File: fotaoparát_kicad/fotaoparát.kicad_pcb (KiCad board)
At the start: 4 copper layers, 102 x 52 mm, 109 parts, among them J1 Conn_01x08_Pin, J13 Micro_SD_Card_Det2, J2 Conn_01x12_Pin, J4 BUTTONS, SW1 SW_MEC_5G, SW2 SW_MEC_5G, U1 TLV62569DBV, Y2 Crystal_GND23

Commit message: FInalni doteky. Ted uz jenom opravy {snad}
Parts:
- removed J2: Conn_01x12_Pin, Connector_FFC-FPC:Hirose_FH12-11S-0.5SH_1x11-1MP_P0.50mm_Horizontal
- removed the R8 at (188.2, 113.7)
- added R50: 330R, Resistor_SMD:R_0603_1608Metric, F.Cu at (188.2, 113.5)
- moved C30 1.57 mm to (139.2, 124.6)
- moved C29 1.57 mm to (138.4, 124.6)
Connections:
- ESP32_P4 pad 49: USB_DATA_N -> /USB_DATA_N
- ESP32_P4 pad 50: USB_DATA_P -> /USB_DATA_P
- ESP32_P4 pad 95: unconnected-(ESP32_P4-GPIO52/ADC-Pad95) -> LED_A
- Y2 pad 3: Net-(ESP32_P4-XTAL_N) -> Net-(ESP32_P4-XTAL_P)
- Y2 pad 4: Net-(ESP32_P4-XTAL_P) -> Net-(ESP32_P4-XTAL_N)
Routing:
- net Net-(J2-Pin_6): track 99.8 -> 0.00 mm, vias 2 -> 0
- net LED_A: track 0.00 -> 99.8 mm, vias 0 -> 2
- net I2C_SDA: track 37.9 -> 63.1 mm, vias 2 -> 3
- net I2C_SCL: track 37.6 -> 62.3 mm, vias 2 -> 3
- net GND: track 168.3 -> 174.2 mm, vias 46 -> 45
- net Net-(ESP32_P4-XTAL_N): track 11.0 -> 15.8 mm
- net Net-(J4-Pin_2): track 0.00 -> 3.65 mm, vias 0 -> 1
- net Net-(J2-Pin_1): track 3.65 -> 0.00 mm, vias 1 -> 0
- net unconnected-(C13-Pad2): track 1.31 -> 2.62 mm, vias 1 -> 2
- net Net-(ESP32_P4-XTAL_P): track 11.8 -> 13.0 mm
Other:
- board size 102 x 52 mm -> 102 x 52.8 mm

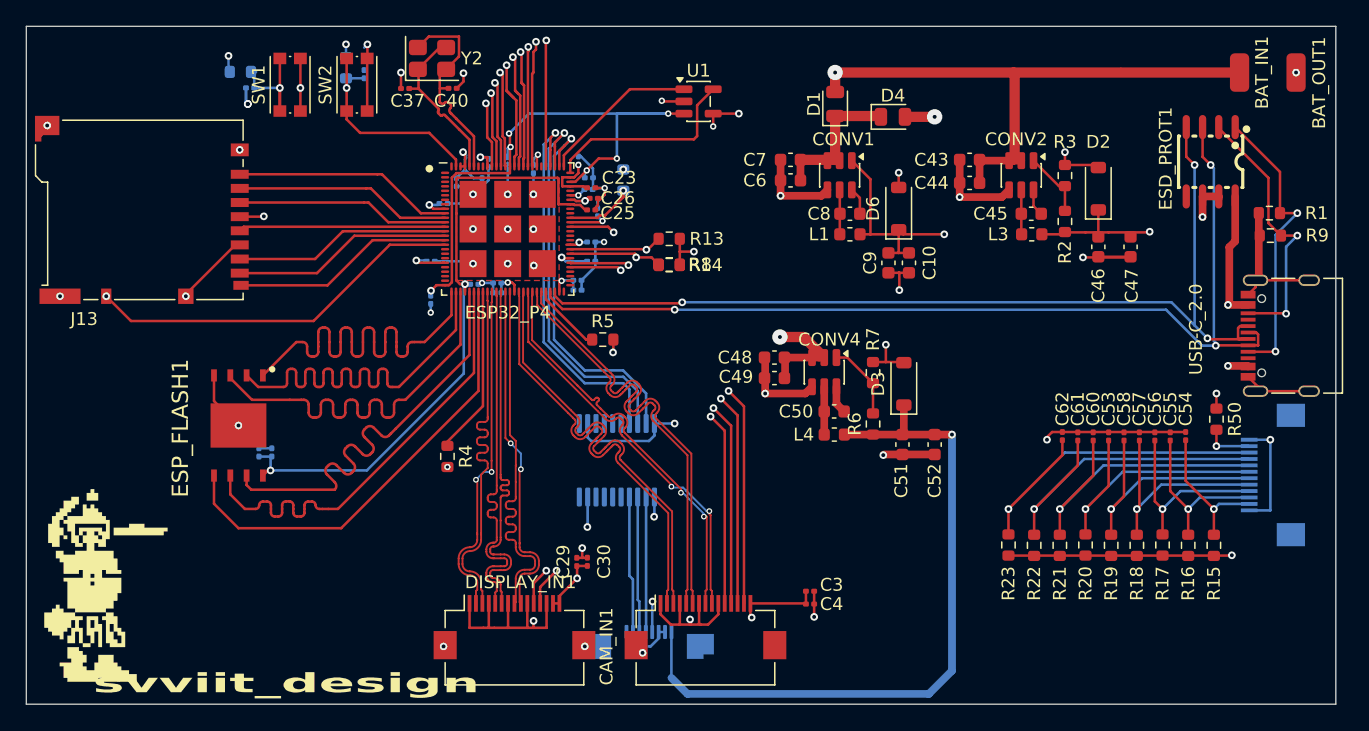
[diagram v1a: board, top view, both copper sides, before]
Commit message: Udelal jsem: -Predelani labelu na global -Pridani vyvodu na desku pro spoust -Pokusil se predelat ten stepdown, Vout by mela byt 1V1, nestihl jsem prepsat vsechny hodnoty a pridat lscs cisla
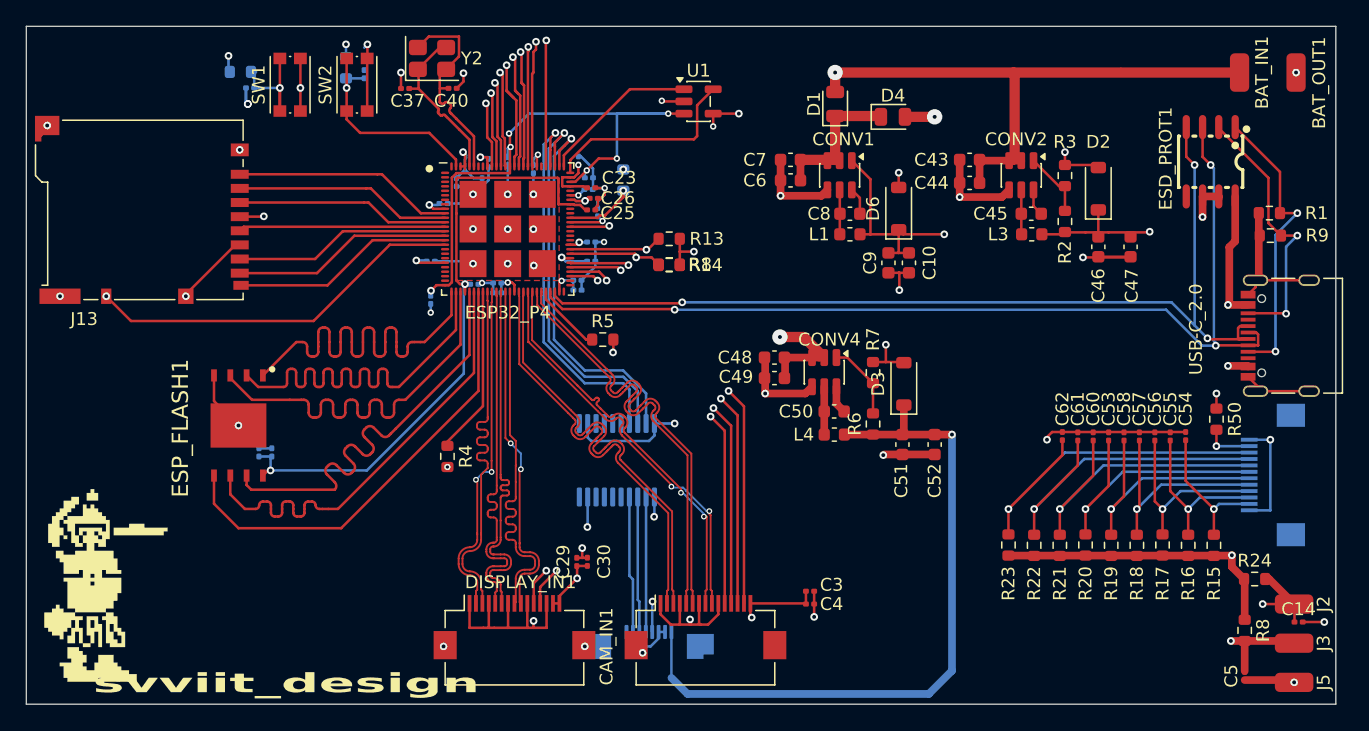
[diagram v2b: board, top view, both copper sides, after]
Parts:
- added C14: 100nF, Capacitor_SMD:C_0201_0603Metric, F.Cu at (194.6, 129.3)
- added C5: 100nF, Capacitor_SMD:C_0201_0603Metric, F.Cu at (190.4, 133.5)
- added J2: Conn_01x01_Socket, Connector_Wire:SolderWirePad_1x01_SMD_1.5x3mm, F.Cu at (194.2, 127.9)
- added J3: Conn_01x01_Socket, Connector_Wire:SolderWirePad_1x01_SMD_1.5x3mm, F.Cu at (194.2, 131.0)
- added J5: Conn_01x01_Socket, Connector_Wire:SolderWirePad_1x01_SMD_1.5x3mm, F.Cu at (194.2, 134.0)
- added R24: 10k, Resistor_SMD:R_0603_1608Metric, F.Cu at (191.2, 126.0)
- added R8: 10k, Resistor_SMD:R_0603_1608Metric, F.Cu at (190.4, 130.0)
- Y2: value Crystal_GND23 -> Crystal_GND24
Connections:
- ESP32_P4 pad 10: /DAT2 -> DAT2
- ESP32_P4 pad 11: /DAT3/CD -> DAT3/CD
- ESP32_P4 pad 12: /CMD -> CMD
- ESP32_P4 pad 13: /CLK -> CLK
- ESP32_P4 pad 14: /DAT0 -> DAT0
- ESP32_P4 pad 15: /DAT1 -> DAT1
- ESP32_P4 pad 16: /DET2 -> DET2
- ESP32_P4 pad 17: /DET1 -> DET1
- ESP32_P4 pad 35: /DSI_DATAP1 -> DSI_DATAP1
- ESP32_P4 pad 36: /DSI_DATAN1 -> DSI_DATAN1
- ESP32_P4 pad 37: /DSI_CLKN -> DSI_CLKN
- ESP32_P4 pad 38: /DSI_CLKP -> DSI_CLKP
- ESP32_P4 pad 39: /DSI_DATAP0 -> DSI_DATAP0
- ESP32_P4 pad 40: /DSI_DATAN0 -> DSI_DATAN0
- ESP32_P4 pad 42: /CSI_DATA_N0 -> CSI_DATA_N0
- ESP32_P4 pad 43: /CSI_DATA_P0 -> CSI_DATA_P0
- ESP32_P4 pad 44: /CSI_CLK_P -> CSI_CLK_P
- ESP32_P4 pad 45: /CSI_CLK_N -> CSI_CLK_N
- ESP32_P4 pad 46: /CSI_DATA_N1 -> CSI_DATA_N1
- ESP32_P4 pad 47: /CSI_DATA_P1 -> CSI_DATA_P1
- ESP32_P4 pad 55: unconnected-(ESP32_P4-GPIO26/ADC/USB-Pad55) -> Net-(ESP32_P4-GPIO26/ADC/USB)
- ESP32_P4 pad 56: unconnected-(ESP32_P4-GPIO27/ADC/USB-Pad56) -> Net-(ESP32_P4-GPIO27/ADC/USB)
- J13 pad 1: /PERIPHERALS/DAT2 -> DAT2
- J13 pad 10: /PERIPHERALS/DET1 -> DET1
- J13 pad 2: /PERIPHERALS/DAT3/CD -> DAT3/CD
- J13 pad 3: /PERIPHERALS/CMD -> CMD
- J13 pad 5: /PERIPHERALS/CLK -> CLK
- J13 pad 7: /PERIPHERALS/DAT0 -> DAT0
- J13 pad 8: /PERIPHERALS/DAT1 -> DAT1
- J13 pad 9: /PERIPHERALS/DET2 -> DET2
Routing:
- net Net-(ESP32_P4-GPIO27/ADC/USB): track 0.00 -> 73.7 mm, vias 0 -> 2
- net Net-(ESP32_P4-GPIO26/ADC/USB): track 0.00 -> 72.6 mm, vias 0 -> 2
- net DSI_DATAN0: track 0.00 -> 29.8 mm
- net /DSI_DATAN0: track 29.8 -> 0.00 mm
- net DSI_CLKP: track 0.00 -> 29.8 mm
- net /DSI_CLKP: track 29.8 -> 0.00 mm
- net DSI_CLKN: track 0.00 -> 29.8 mm
- net /DSI_CLKN: track 29.8 -> 0.00 mm
- net DSI_DATAP1: track 0.00 -> 29.8 mm
- net /DSI_DATAP1: track 29.8 -> 0.00 mm
- net DET1: track 0.00 -> 29.7 mm, vias 0 -> 1
- net /DET1: track 29.7 -> 0.00 mm, vias 1 -> 0
- net DSI_DATAP0: track 0.00 -> 26.9 mm, vias 0 -> 2
- net /DSI_DATAP0: track 26.9 -> 0.00 mm, vias 2 -> 0
- net DSI_DATAN1: track 0.00 -> 26.8 mm, vias 0 -> 2
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
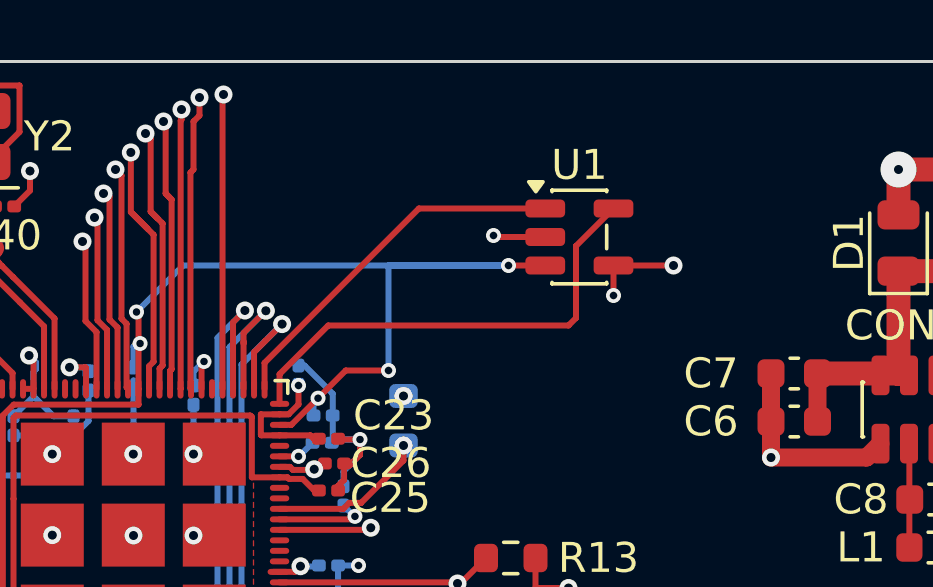
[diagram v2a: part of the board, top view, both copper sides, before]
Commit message: Dodelani stepdownu, prirazeni lscs cisel
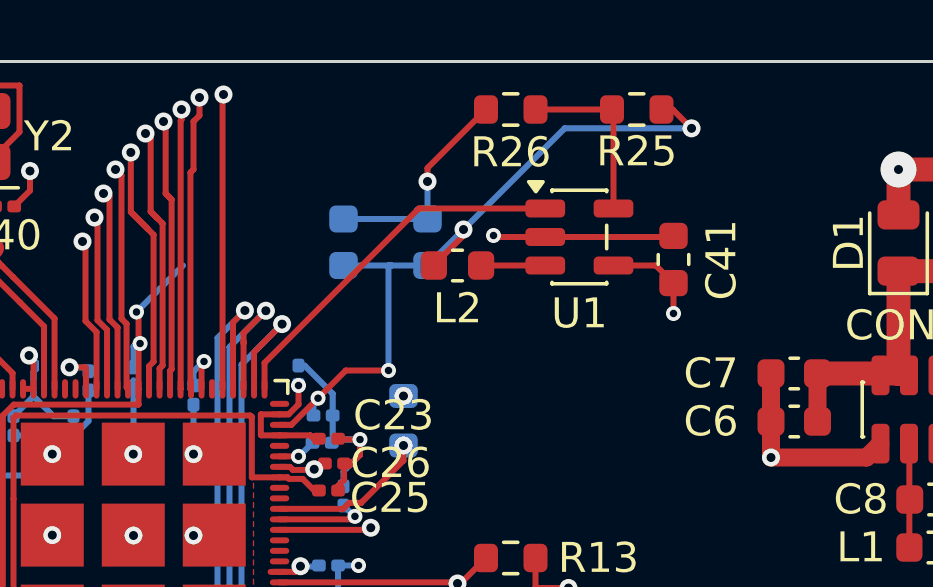
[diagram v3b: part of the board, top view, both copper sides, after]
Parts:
- added C15: 22uF, Capacitor_SMD:C_0603_1608Metric, B.Cu at (142.8, 88.9)
- added C41: 4.7uF, Inductor_SMD:L_0603_1608Metric, F.Cu at (151.0, 89.5)
- added C42: 22uF, Capacitor_SMD:C_0603_1608Metric, B.Cu at (140.0, 88.9)
- added L2: 2.2uH, Inductor_SMD:L_0603_1608Metric, F.Cu at (143.8, 89.7)
- added R25: 167k, Resistor_SMD:R_0603_1608Metric, F.Cu at (149.8, 84.5)
- added R26: 200k, Resistor_SMD:R_0603_1608Metric, F.Cu at (145.6, 84.5)
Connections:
- ESP32_P4 pad 78: Net-(ESP32_P4-FB_DCDC) -> unconnected-(ESP32_P4-FB_DCDC-Pad78)
- U1 pad 3: /ESP_VDD_HP -> Net-(U1-SW)
- U1 pad 5: Net-(ESP32_P4-FB_DCDC) -> Net-(U1-FB)
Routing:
- net Net-(ESP32_P4-FB_DCDC): track 15.8 -> 0.00 mm
- net GND: track 179.8 -> 191.5 mm, vias 47 -> 48
- net Net-(U1-FB): track 0.00 -> 5.87 mm
- net Net-(U1-SW): track 0.00 -> 2.14 mm
- net /ESP_VDD_HP: track 46.3 -> 46.7 mm, vias 6 -> 7
- net +3V3: track 93.4 -> 93.6 mm, vias 20 -> 19

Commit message: nejaky maly zmeny asi
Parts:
- removed R14: 4k7, Resistor_SMD:R_0603_1608Metric
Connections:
- SW1 pad 2: Net-(ESP32_P4-GPIO35) -> GND
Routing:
- net /ESP_VDD_HP: track 46.7 -> 52.1 mm
- net Net-(ESP32_P4-GPIO35): track 49.3 -> 45.2 mm, vias 3 -> 2
- net GND: track 191.5 -> 195.5 mm, vias 48 -> 49
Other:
- board text removed: "${REFERENCE}"
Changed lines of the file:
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@@
 		)
 	)
-	(footprint "Resistor_SMD:R_0603_1608Metric"
-		(layer "F.Cu")
-		(at 145.551823 101.507979 180)
-		(descr "Resistor SMD 0603 (1608 Metric), square (rectangular) end terminal, IPC-7351 nominal, (Body size source: IPC-SM-782 page 72, https://www.pcb-3d.com/wordpress/wp-content/uploads/ipc-sm-782a_amendment_1_and_2.pdf), generated with kicad-footprint-generator")
-		(tags "resistor")
-		(property "Reference" "R14"
-			(at -2.825 0 0)
-			(layer "F.SilkS")
-			(effects
-				(font
-					(size 1 1)
-					(thickness 0.15)
-				)
-			)
-		)
-		(property "Value" "4k7"
-			(at 0 1.43 0)
-			(layer "F.Fab")
-			(effects
-				(font
-					(size 1 1)
-					(thickness 0.15)
-				)
-			)
-		)
-		(property "Datasheet" "~"
-			(at 0 0 0)
-			(layer "F.Fab")
-			(hide yes)
-			(effects
-				(font
-					(size 1.27 1.27)
-					(thickness 0.15)
-				)
-			)
-		)
-		(property "Description" "Resistor"
-			(at 0 0 0)
-			(layer "F.Fab")
-			(hide yes)
-			(effects
-				(font
-					(size 1.27 1.27)
-					(thickness 0.15)
-				)
-			)
-		)
-		(property "LSCS Number" "C14675"
-			(at 0 0 180)
-			(unlocked yes)
-			(layer "F.Fab")
-			(hide yes)
-			(effects
-				(font
-					(size 1 1)
-					(thickness 0.15)
-				)
-			)
-		)
-		(property ki_fp_filters "R_*")
-		(sheetname "/")
-		(sheetfile "fotaoparát.kicad_sch")
-		(attr smd)
-		(fp_line
-			(start -0.237258 0.5225)
-			(end 0.237258 0.5225)
-			(stroke
-				(width 0.12)
-				(type solid)
-			)
-			(layer "F.SilkS")
-		)
-		(fp_line
-			(start -0.237258 -0.5225)
-			(end 0.237258 -0.5225)
-			(stroke
-				(width 0.12)
-				(type solid)
-			)
-			(layer "F.SilkS")
-		)
-		(fp_line
-			(start 1.48 0.73)
-			(end -1.48 0.73)
-			(stroke
-				(width 0.05)
-				(type solid)
-			)
-			(layer "F.CrtYd")
-		)
-		(fp_line
-			(start 1.48 -0.73)
-			(end 1.48 0.73)
-			(stroke
-				(width 0.05)
-				(type solid)
-			)
-			(layer "F.CrtYd")
-		)
-		(fp_line
-			(start -1.48 0.73)
-			(end -1.48 -0.73)
-			(stroke
-				(width 0.05)
-				(type solid)
-			)
-			(layer "F.CrtYd")
-		)
-		(fp_line
-			(start -1.48 -0.73)
-			(end 1.48 -0.73)
-			(stroke
-				(width 0.05)
-				(type solid)
-			)
-			(layer "F.CrtYd")
-		)
-		(fp_line
-			(start 0.8 0.4125)
-			(end -0.8 0.4125)
-			(stroke
-				(width 0.1)
-				(type solid)
-			)
-			(layer "F.Fab")
-		)
-		(fp_line
-			(start 0.8 -0.4125)
-			(end 0.8 0.4125)
-			(stroke
-				(width 0.1)
-				(type solid)
-			)
-			(layer "F.Fab")
-		)
-		(fp_line
-			(start -0.8 0.4125)
-			(end -0.8 -0.4125)
-			(stroke
-				(width 0.1)
-				(type solid)
-			)
-			(layer "F.Fab")
-		)
-		(fp_line
-			(start -0.8 -0.4125)
-			(end 0.8 -0.4125)
-			(stroke
-				(width 0.1)
-				(type solid)
-			)
-			(layer "F.Fab")
-		)
-		(fp_text user "${REFERENCE}"
-			(at 0 0 0)
-			(layer "F.Fab")
-			(effects
-				(font
-					(size 0.4 0.4)
-					(thickness 0.06)
-				)
-			)
-		)
-		(pad "1" smd roundrect
-			(at -0.825 0 180)
-			(size 0.8 0.95)
-			(layers "F.Cu" "F.Mask" "F.Paste")
-			(roundrect_rratio 0.25)
-			(net 45 "+3V3")
-			(pintype "passive")
-		)
-		(pad "2" smd roundrect
-			(at 0.825 0 180)
-			(size 0.8 0.95)
-			(layers "F.Cu" "F.Mask" "F.Paste")
-			(roundrect_rratio 0.25)
-			(net 86 "I2C_SCL")
-			(pintype "passive")
-		)
-		(embedded_fonts no)
-		(model "${KICAD9_3DMODEL_DIR}/Resistor_SMD.3dshapes/R_0603_1608Metric.step"
-			(offset
-				(xyz 0 0 0)
-			)
-			(scale
-				(xyz 1 1 1)
-			)
-			(rotate
-				(xyz 0 0 0)
-			)
-		)
-	)
 	(footprint "Capacitor_SMD:C_0201_0603Metric"
 		(layer "F.Cu")
@@
 			(size 0.9 1)
 			(layers "F.Cu" "F.Mask" "F.Paste")
-			(net 6 "Net-(ESP32_P4-GPIO35)")
+			(net 1 "GND")
 			(pinfunction "A")
 			(pintype "passive")
@@
 			(size 0.9 1)
 			(layers "F.Cu" "F.Mask" "F.Paste")
-			(net 6 "Net-(ESP32_P4-GPIO35)")
+			(net 1 "GND")
 			(pinfunction "A")
 			(pintype "passive")
@@
 		(tags "resistor")
 		(property "Reference" "R8"
-			(at -2.425 0 0)
+			(at -2.425 -0.05 0)
 			(layer "F.SilkS")
 			(effects
@@
 		(layer "Edge.Cuts")
 	)
-	(gr_text "${REFERENCE}"
-		(at 156.601823 130.675 0)
-		(layer "B.Fab")
-		(effects
-			(font
-				(size 1 1)
-				(thickness 0.15)
-			)
-			(justify mirror)
-		)
-	)
 	(segment
 		(start 154.226823 96.107979)
@@
 	)
 	(segment
+		(start 116.826823 89.507979)
+		(end 116.826823 85.407979)
+		(width 0.2)
+		(layer "F.Cu")
+		(net 1)
+	)
+	(segment
 		(start 174.976823 115.107979)
 		(end 174.976823 114.907979)
@@
 	)
 	(segment
+		(start 116.826823 89.507979)
+		(end 116.826823 89.457979)
+		(width 0.2)
+		(layer "F.Cu")
+		(net 1)
+	)
+	(segment
 		(start 136 129.757979)
 		(end 136 127.857979)
@@
 	)
 	(via
+		(at 116.826823 87.707979)
+		(size 0.6)
+		(drill 0.3)
+		(layers "F.Cu" "B.Cu")
+		(free yes)
+		(net 1)
+	)
+	(via
 		(at 144.976823 88.707979)
 		(size 0.5)
@@
 	)
 	(segment
-		(start 132.976823 93.527979)
-		(end 132.976823 95.988177)
-		(width 0.2)
-		(layer "B.Cu")
-		(net 1)
-	)
-	(segment
 		(start 139.796823 101.207979)
 		(end 139.796823 99.707979)
@@
 	)
 	(segment
+		(start 132.976823 95.988177)
+		(end 132.97 95.995)
+		(width 0.2)
+		(layer "B.Cu")
+		(net 1)
+	)
+	(segment
 		(start 126.976823 104.527979)
 		(end 126.976823 105.207979)
@@
 	)
 	(segment
-		(start 132.976823 95.988177)
-		(end 132.97 95.995)
-		(width 0.2)
-		(layer "B.Cu")
-		(net 1)
-	)
-	(segment
 		(start 113.5975 115.5975)
 		(end 112 114)
@@
 	)
 	(segment
+		(start 132.976823 93.747979)
+		(end 132.976823 95.988177)
+		(width 0.2)
+		(layer "B.Cu")
+		(net 1)
+	)
+	(segment
 		(start 131.836823 102.897509)
 		(end 131.836823 103.662172)
@@
 	)
 	(segment
-		(start 116.826823 89.507979)
-		(end 116.826823 85.407979)
-		(width 0.2)
-		(layer "F.Cu")
-		(net 6)
-	)
-	(segment
-		(start 116.826823 89.507979)
-		(end 116.826823 89.457979)
-		(width 0.2)
-		(layer "F.Cu")
-		(net 6)
-	)
-	(segment
 		(start 115.226823 89.507979)
 		(end 115.226823 85.407979)
@@
 		(net 6)
 	)
-	(via
-		(at 116.826823 87.707979)
-		(size 0.6)
-		(drill 0.3)
-		(layers "F.Cu" "B.Cu")
-		(net 6)
-	)
 	(segment
 		(start 113.226823 87.707979)
@@
 		(width 0.2)
 		(layer "B.Cu")
+		(net 101)
+	)
+	(segment
+		(start 134.626823 89.707979)
+		(end 139.976823 89.707979)
+		(width 0.2)
+		(layer "B.Cu")
